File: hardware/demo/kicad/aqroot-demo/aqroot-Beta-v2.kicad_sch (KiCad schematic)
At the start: 0 parts

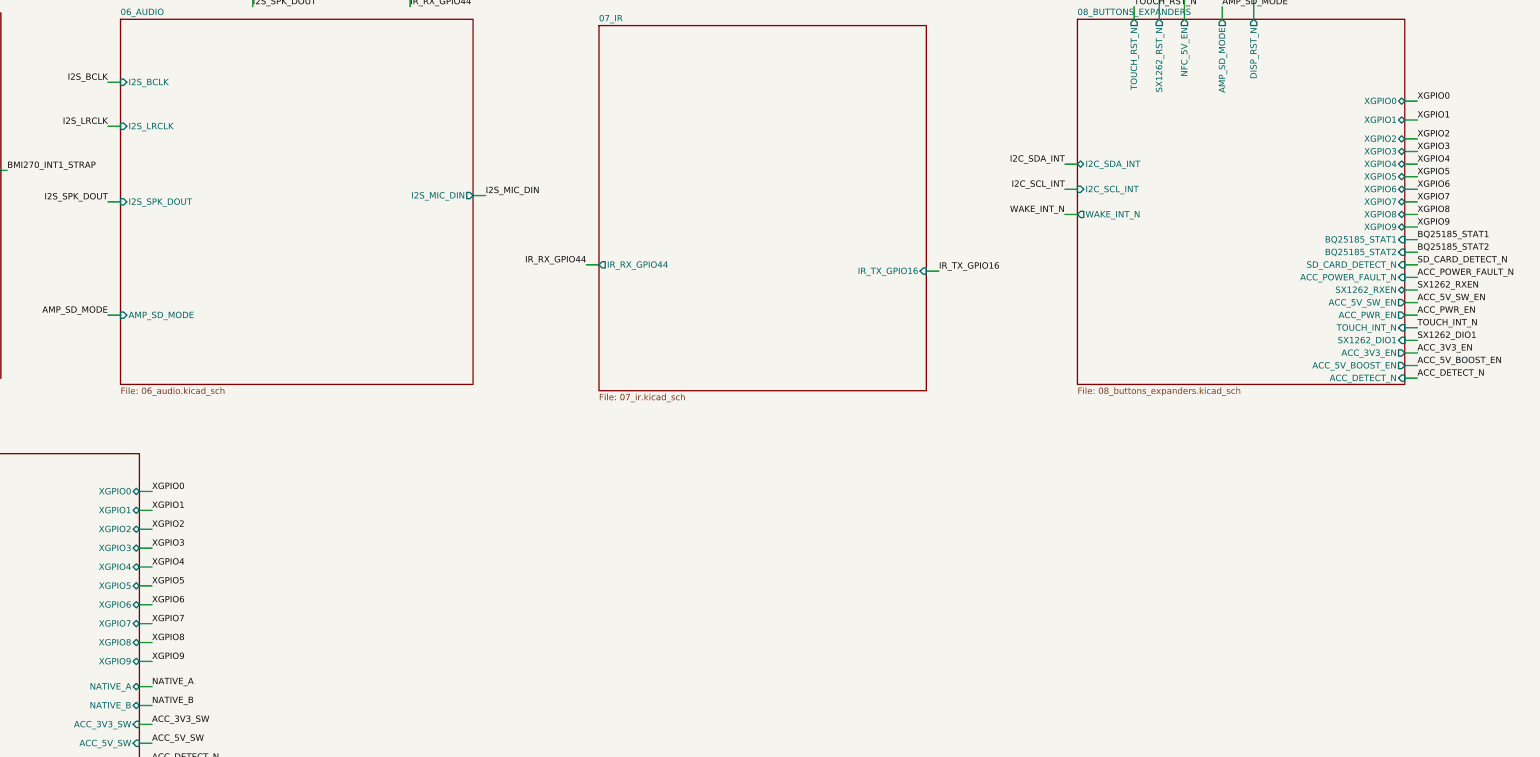
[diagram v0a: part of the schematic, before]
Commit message: demo: apply schematic simplification ECO
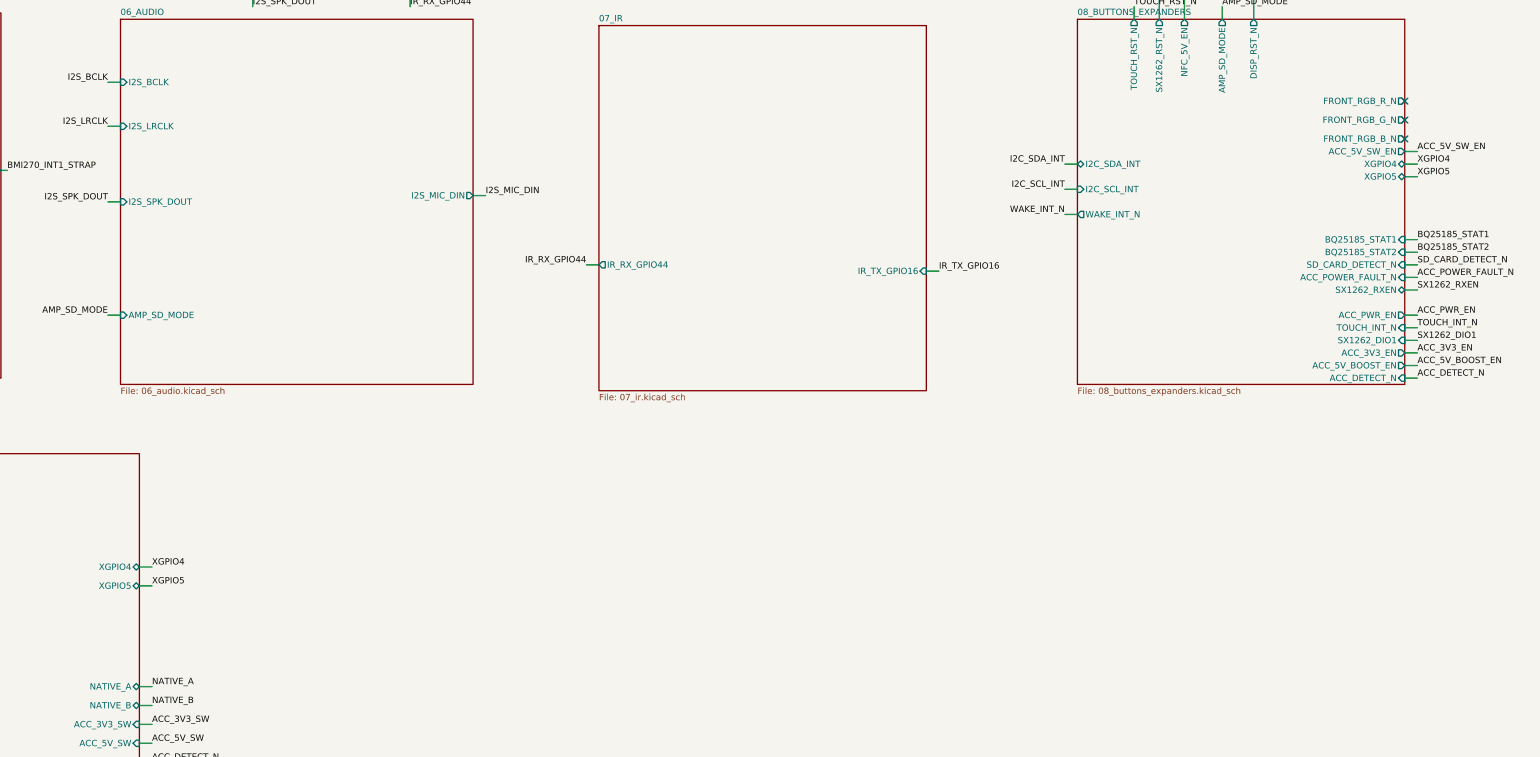
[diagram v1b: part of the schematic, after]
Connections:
- no-connect marks 0 -> 3
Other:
- sheet 08_BUTTONS_EXPANDERS ports: added FRONT_RGB_B_N, FRONT_RGB_G_N, FRONT_RGB_R_N; removed XGPIO0, XGPIO1, XGPIO2, XGPIO3, XGPIO6, XGPIO7, XGPIO8, XGPIO9
- sheet 09_COMMUNITY_HEADER ports: added none; removed XGPIO0, XGPIO1, XGPIO2, XGPIO3, XGPIO6, XGPIO7, XGPIO8, XGPIO9
